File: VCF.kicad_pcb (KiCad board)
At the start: 2 copper layers, 55 x 100 mm, 53 parts, among them J1 CV_IN, J2 TP_OUT, J3 BP_OUT, J4 HP_OUT, U1 TL084, U2 TL084, U3 CA3080, U4 CA3080

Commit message: Add files via upload
First Layout Draft (Not Complete!) 
Current File: VCF. Only for measuring the layout
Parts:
- added H2: MountingHole_Pad, MountingHole:MountingHole_3.2mm_M3_DIN965_Pad, F.Cu at (57.5, 54.0)
- added J5: AUDIO_IN, Connector_Audio:Jack_3.5mm_QingPu_WQP-PJ398SM_Vertical_CircularHoles, F.Cu at (58.4, 135.3)
- added RV3: 100k, Potentiometer_THT:Potentiometer_Alpha_RD901F-40-00D_Single_Vertical_CircularHoles, F.Cu at (55.9, 94.6)
- added RV4: 100k, Potentiometer_THT:Potentiometer_Alpha_RD901F-40-00D_Single_Vertical_CircularHoles, F.Cu at (157.5, 76.6)
- C1, C15, C16, C2, R1, R12, R13, R14, R15, R16, R19, R2, R20, R21, R23, R24, R25, R26, R27, R28, R3, R4, R5, R6, R7, R8, R9, U1, U2, U3, U4: moved to B.Cu
- C14: renamed from C3; moved to B.Cu
- C3: renamed from C12; moved to B.Cu
- H1: moved to F.Cu
- moved RV2 161.5 mm to (55.9, 76.8), turned to 90 degrees
- moved R5 138.5 mm to (133.9, 135.4), turned to 90 degrees
- moved C2 134.4 mm to (139.4, 127.5), turned to 90 degrees
- moved R12 133.2 mm to (134.1, 87.4), turned to 90 degrees
- moved R14 124.6 mm to (130.8, 87.4), turned to 90 degrees
- moved R22 121.4 mm to (133.9, 119.6), turned to 90 degrees
- moved R24 108.8 mm to (154.7, 105.9), turned to 90 degrees
- moved R2 105.4 mm to (159.0, 111.5), turned to -90 degrees
- moved R3 103.8 mm to (162.1, 121.7), turned to 90 degrees
- moved R19 102.5 mm to (154.7, 91.2), turned to 90 degrees
- moved C3 96.8 mm to (155.2, 127.5), turned to 90 degrees
- moved R21 96.2 mm to (158.0, 81.0), turned to -90 degrees
- moved R1 91.0 mm to (137.2, 100.6), turned to 90 degrees
- moved R10 90.7 mm to (162.8, 134.9), turned to 90 degrees
- moved R20 89.5 mm to (161.3, 105.9), turned to 90 degrees
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- renumbered C13 to C12, C14 to C13
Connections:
- C14 pad 1: /AUDIO_IN -> Net-(C14-Pad1)
- C3 pad 2: Net-(C12-Pad2) -> Net-(C3-Pad2)
- R14 pad 1: /BP -> Net-(RV4-Pad3)
- U1 pad 1: Net-(R6-Pad1) -> /TP_OUT
- U1 pad 10: Net-(C12-Pad2) -> Net-(R4-Pad2)
- U1 pad 12: Net-(R4-Pad2) -> Net-(R22-Pad1)
- U1 pad 13: Net-(C2-Pad2) -> Net-(R27-Pad2)
- U1 pad 14: /HP_OUT -> /Bias
- U1 pad 2: Net-(R1-Pad1) -> Net-(R2-Pad2)
- U1 pad 3: GND -> Net-(C1-Pad2)
- U1 pad 5: Net-(C1-Pad2) -> Net-(C3-Pad2)
- U1 pad 6: Net-(R2-Pad2) -> Net-(R10-Pad2)
- U1 pad 7: /TP_OUT -> /BP_OUT
- U1 pad 8: /BP_OUT -> /HP_OUT
- U1 pad 9: Net-(R10-Pad2) -> Net-(C2-Pad2)
- U2 pad 1: /Bias -> /BP
- U2 pad 10: Net-(C15-Pad1) -> GND
- U2 pad 12: /TP -> Net-(R14-Pad2)
- U2 pad 13: Net-(C16-Pad1) -> Net-(R20-Pad2)
- U2 pad 14: /TP -> /HP
- U2 pad 2: Net-(R27-Pad2) -> /BP
- U2 pad 3: Net-(R22-Pad1) -> Net-(C15-Pad1)
- U2 pad 5: Net-(R14-Pad2) -> /TP
- U2 pad 6: Net-(R20-Pad2) -> Net-(C16-Pad1)
- U2 pad 7: /HP -> /TP
- U2 pad 8: /BP -> Net-(R6-Pad1)
- U2 pad 9: /BP -> Net-(R1-Pad1)
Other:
- board size 55 x 100 mm -> 58 x 105 mm

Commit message: Poti Positioning
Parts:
- H2: footprint MountingHole:MountingHole_3.2mm_M3_DIN965_Pad -> MountingHole:MountingHole_3.2mm_M3_DIN965_Pad_TopBottom
- moved RV4 62.2 mm to (95.3, 75.6)
- moved J1 16.6 mm to (57.1, 134.1)
- moved J5 15.3 mm to (57.1, 150.6)
- moved J2 1.91 mm to (97.8, 150.6)
- moved RV1 1.80 mm to (54.6, 111.1)
- moved RV2 1.80 mm to (54.6, 75.6)
- moved RV3 1.80 mm to (54.6, 93.4)
- moved H1 1.40 mm to (102.9, 53.3)
- moved J3 1.27 mm to (85.1, 150.6)
- moved J4 1.27 mm to (72.4, 150.6)
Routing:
- added copper zone on B.Cu, net GND

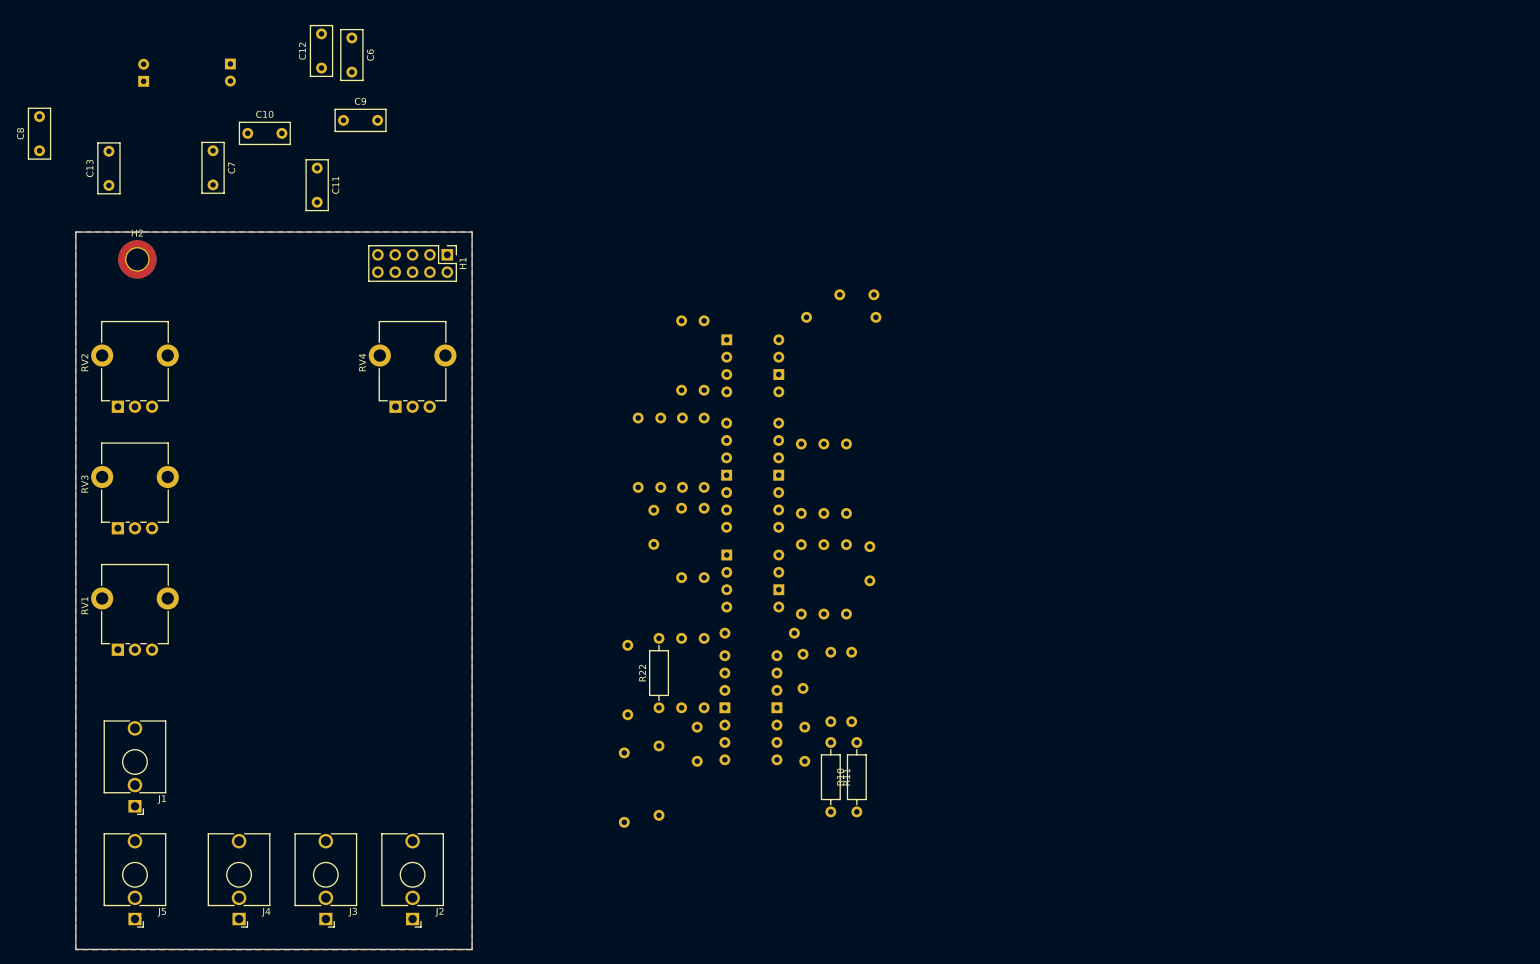
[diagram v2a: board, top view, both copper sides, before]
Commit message: Prototype #1
Layout and Schematics Done. 
Please ignore Silkscreen, SolderPaste and Courtyard warnings; won't be manufactured! 
Check M3 mounting hole size and position and the GND Vias!
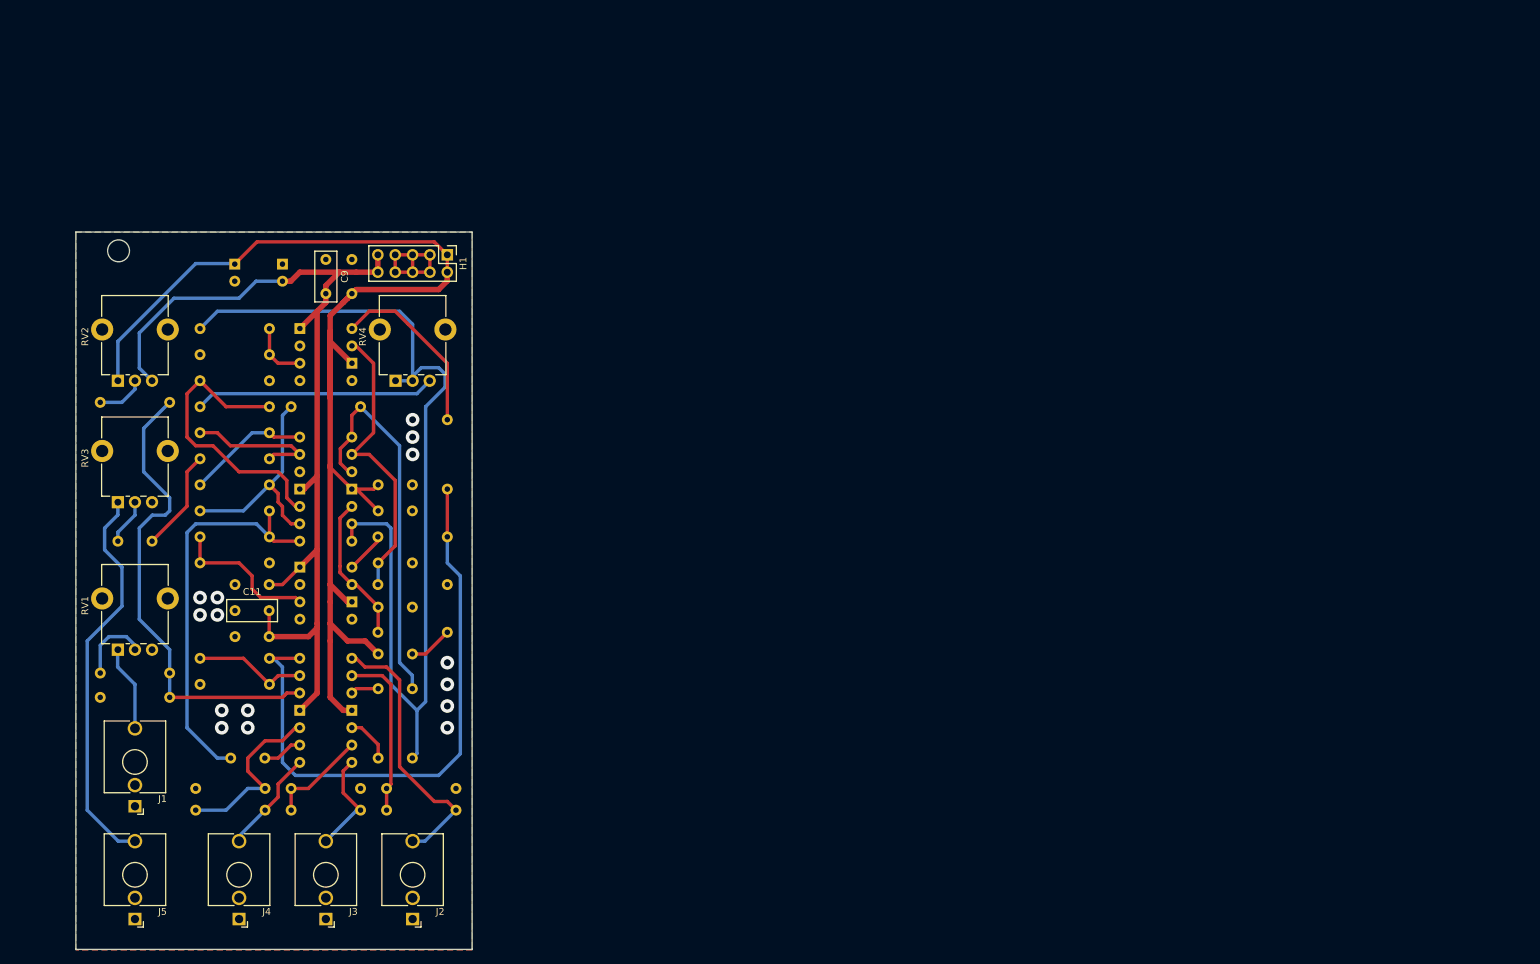
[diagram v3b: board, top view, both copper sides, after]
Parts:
- C10, C12, C13, C6, C7, C8, R10, R11, R22: moved to B.Cu
- H2: footprint MountingHole:MountingHole_3.2mm_M3_DIN965_Pad_TopBottom -> MountingHole:MountingHole_3.2mm_M3_DIN965
- moved R21 92.2 mm to (66.7, 67.9), turned to 0 degrees
- moved R19 92.1 mm to (66.7, 64.1), turned to 0 degrees
- moved C6 90.3 mm to (92.8, 111.8), turned to 0 degrees
- moved C15 81.6 mm to (92.8, 104.9)
- moved R23 81.2 mm to (62.2, 74.9), turned to 180 degrees
- moved R11 79.3 mm to (80.0, 131.4), turned to 0 degrees
- moved R25 78.2 mm to (62.2, 118.1), turned to 180 degrees
- moved R16 77.9 mm to (102.9, 108.6)
- moved R20 77.3 mm to (90.2, 75.6), turned to 180 degrees
- moved C14 73.4 mm to (59.6, 95.2), turned to 180 degrees
- moved R13 72.8 mm to (76.8, 98.4), turned to 180 degrees
- moved R10 72.6 mm to (90.2, 134.6), turned to 180 degrees
- moved R1 72.6 mm to (66.7, 83.2), turned to 0 degrees
- moved C8 72.4 mm to (92.8, 90.8), turned to 0 degrees
- moved C16 72.0 mm to (92.8, 98.4), turned to 0 degrees
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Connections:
- C2 pad 1: /HP -> Net-(C2-Pad1)
- C2 pad 2: Net-(C2-Pad2) -> /HP
- R1 pad 1: Net-(R1-Pad1) -> Net-(C14-Pad1)
- R1 pad 2: Net-(C14-Pad2) -> Net-(R1-Pad2)
- R19 pad 1: Net-(R19-Pad1) -> /BP
- R19 pad 2: /BP -> Net-(R19-Pad2)
- R21 pad 2: Net-(R19-Pad1) -> Net-(R19-Pad2)
- R27 pad 1: /Bias -> /BIAS
- R6 pad 2: Net-(R1-Pad1) -> Net-(R1-Pad2)
- R8 pad 1: Net-(R14-Pad2) -> Net-(R14-Pad1)
- RV3 pad 2: Net-(C14-Pad1) -> Net-(C14-Pad2)
- RV4 pad 3: Net-(R14-Pad1) -> Net-(R14-Pad2)
- U1 pad 14: /Bias -> /BIAS
- U1 pad 9: Net-(C2-Pad2) -> Net-(C2-Pad1)
- U2 pad 1: /BP -> /TP
- U2 pad 10: GND -> Net-(R14-Pad1)
- U2 pad 12: Net-(R14-Pad2) -> GND
- U2 pad 13: Net-(R20-Pad2) -> Net-(R1-Pad2)
- U2 pad 14: /HP -> Net-(R6-Pad1)
- U2 pad 2: /BP -> Net-(C16-Pad1)
- U2 pad 3: Net-(C15-Pad1) -> /TP
- U2 pad 5: /TP -> Net-(C15-Pad1)
- U2 pad 6: Net-(C16-Pad1) -> /BP
- U2 pad 7: /TP -> /BP
- U2 pad 8: Net-(R6-Pad1) -> /HP
- U2 pad 9: Net-(R1-Pad1) -> Net-(R20-Pad2)
- U4 pad 2: Net-(R19-Pad1) -> Net-(R19-Pad2)
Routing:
- net +12V: track 0.00 -> 186.9 mm
- net /BP: track 0.00 -> 145.0 mm
- net -12V: track 0.00 -> 142.9 mm
- net /BIAS: track 0.00 -> 88.5 mm
- net Net-(R22-Pad1): track 0.00 -> 70.4 mm
- net /HP: track 0.00 -> 58.7 mm
- net /AUDIO_IN_ATT: track 0.00 -> 57.9 mm
- net /TP: track 0.00 -> 56.1 mm
- net Net-(C16-Pad1): track 0.00 -> 43.1 mm
- net Net-(R14-Pad1): track 0.00 -> 43.0 mm
- net /TP_OUT: track 0.00 -> 40.1 mm
- net Net-(R14-Pad2): track 0.00 -> 35.2 mm
- net Net-(R20-Pad2): track 0.00 -> 32.8 mm
- net Net-(R4-Pad2): track 0.00 -> 26.4 mm
- net Net-(R24-Pad2): track 0.00 -> 26.4 mm
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
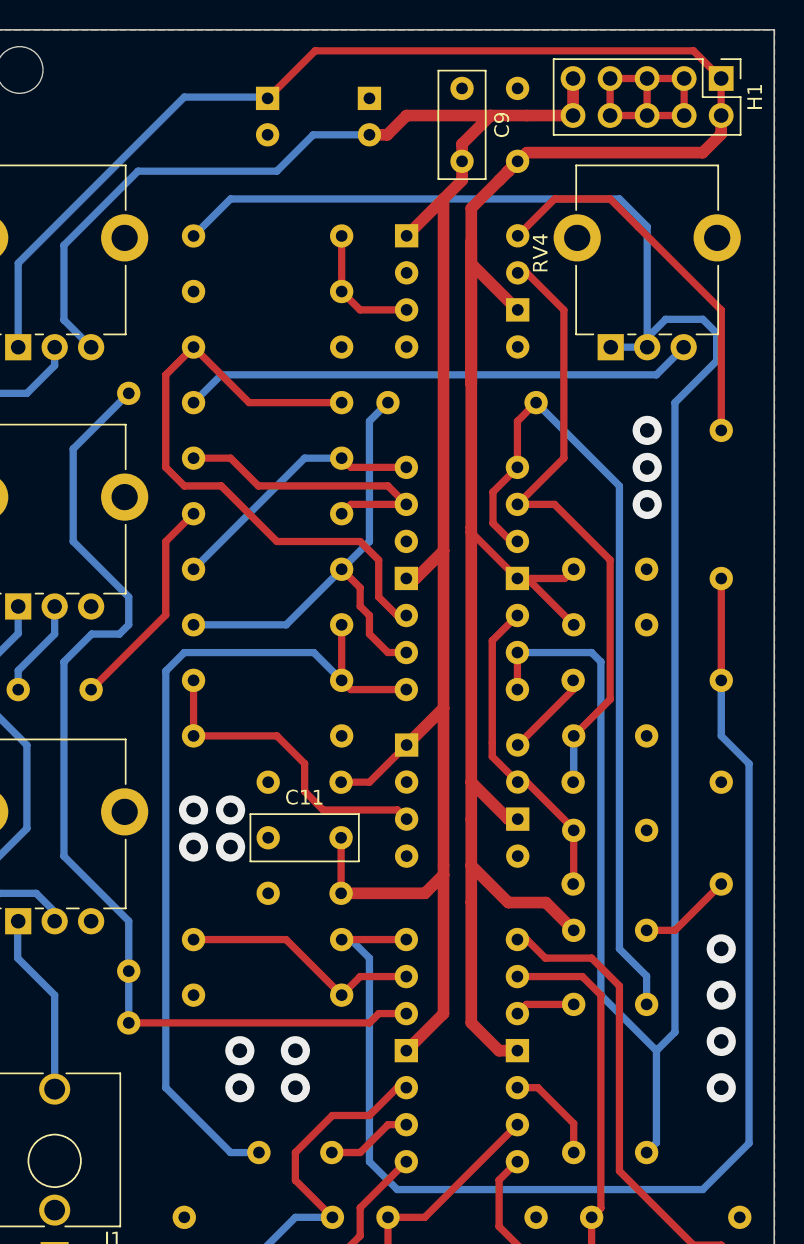
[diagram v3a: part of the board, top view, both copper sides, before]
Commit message: Add files via upload
Updated Capacitors to be all on on the bottom layer and all it's conducting paths on the top layer. This uses two VIAs extra VIAs for the signal paths.
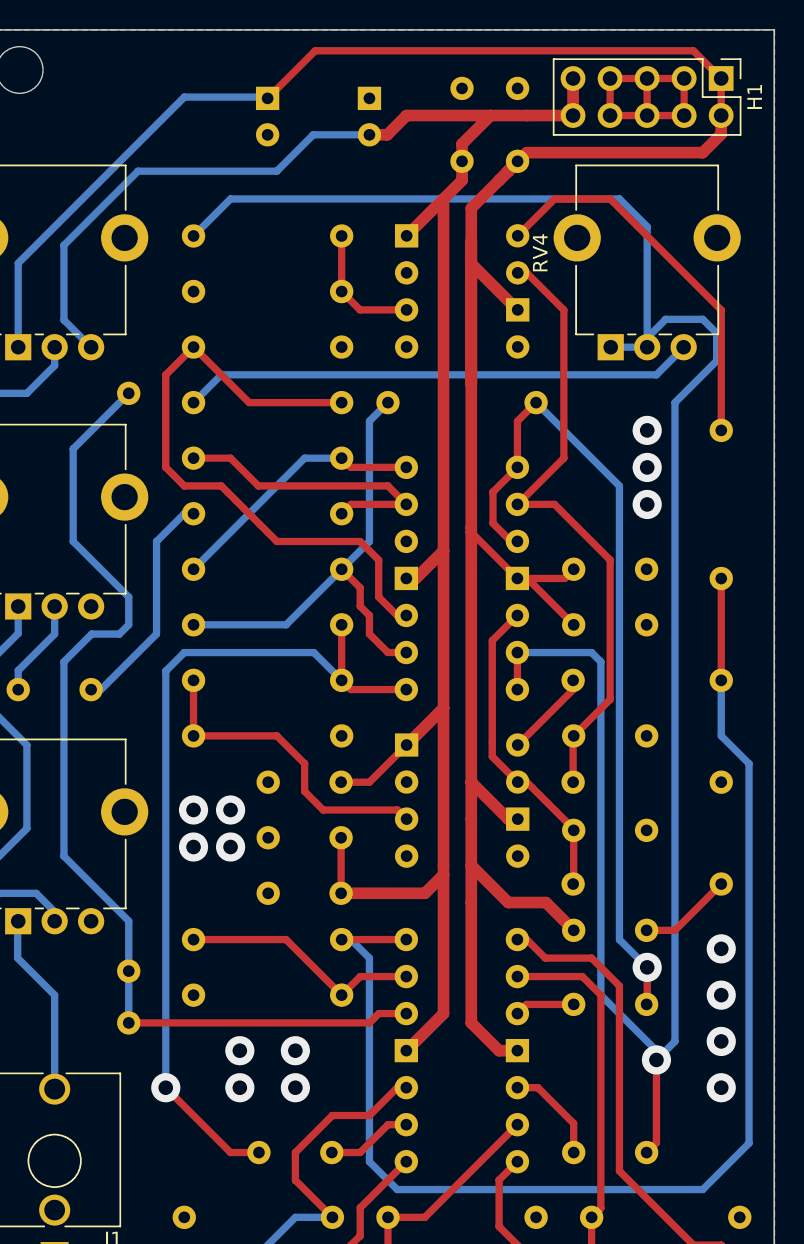
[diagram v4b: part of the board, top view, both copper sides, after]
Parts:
- C11, C9: moved to B.Cu
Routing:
- net Net-(C14-Pad1): track 15.0 -> 15.7 mm
- net /BP: track 145.0 -> 145.6 mm, vias 0 -> 1
- net /TP: vias 0 -> 1
- net /HP: vias 0 -> 1
